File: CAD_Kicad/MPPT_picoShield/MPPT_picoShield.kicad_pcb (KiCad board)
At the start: 2 copper layers, 95 x 65 mm, 61 parts, among them J1 PV_input, J2 Battery_pack, J3 V_out, J4 Micro_SD_Card_Det_Hirose_DM3AT, J5 GPIO breakout, Q1 PMOS_GDS_TO220, Q2 NMOS_DGS_SOT23, Q3 NMOS_DGS_SOT23, SW1 RESET, U1 RaspiPico, U10 LF50_TO220, U2 INA3221

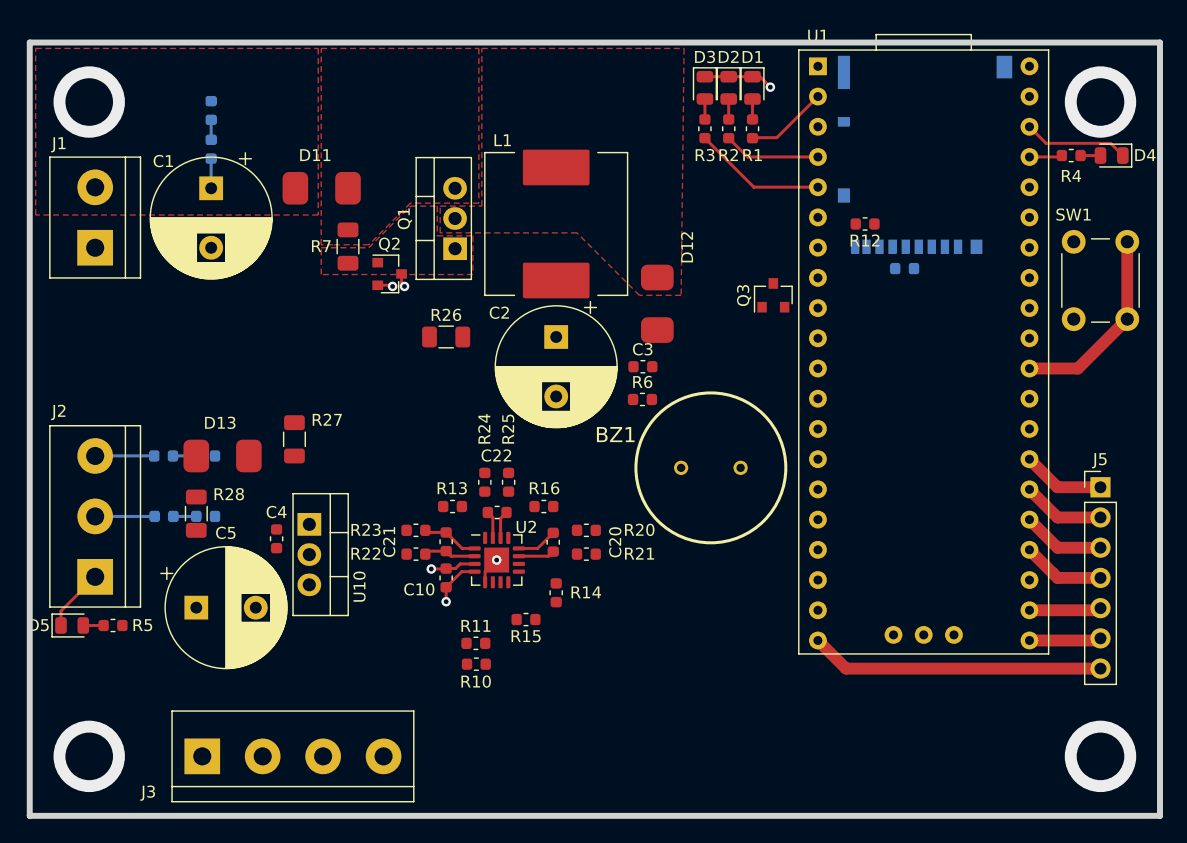
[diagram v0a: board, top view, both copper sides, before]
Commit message: Initial routing
Small verifications to be made: 
- Should Metal of INA2331 be connected to ground? Or a floating metal plane? or Vcc?
- Should capacitors be added to the long analog lines to stabilize them?
- Should D11 and its polarized cap be swapped to "idiot proof" the PV connector?
- Rasp Pico silkscreen is outside of PCB, should probably fix that
- Indicator of pin 1 on INA2331 is overlapping a via, small esthetic fix to be made
- Note for future: DPAK or TO220?
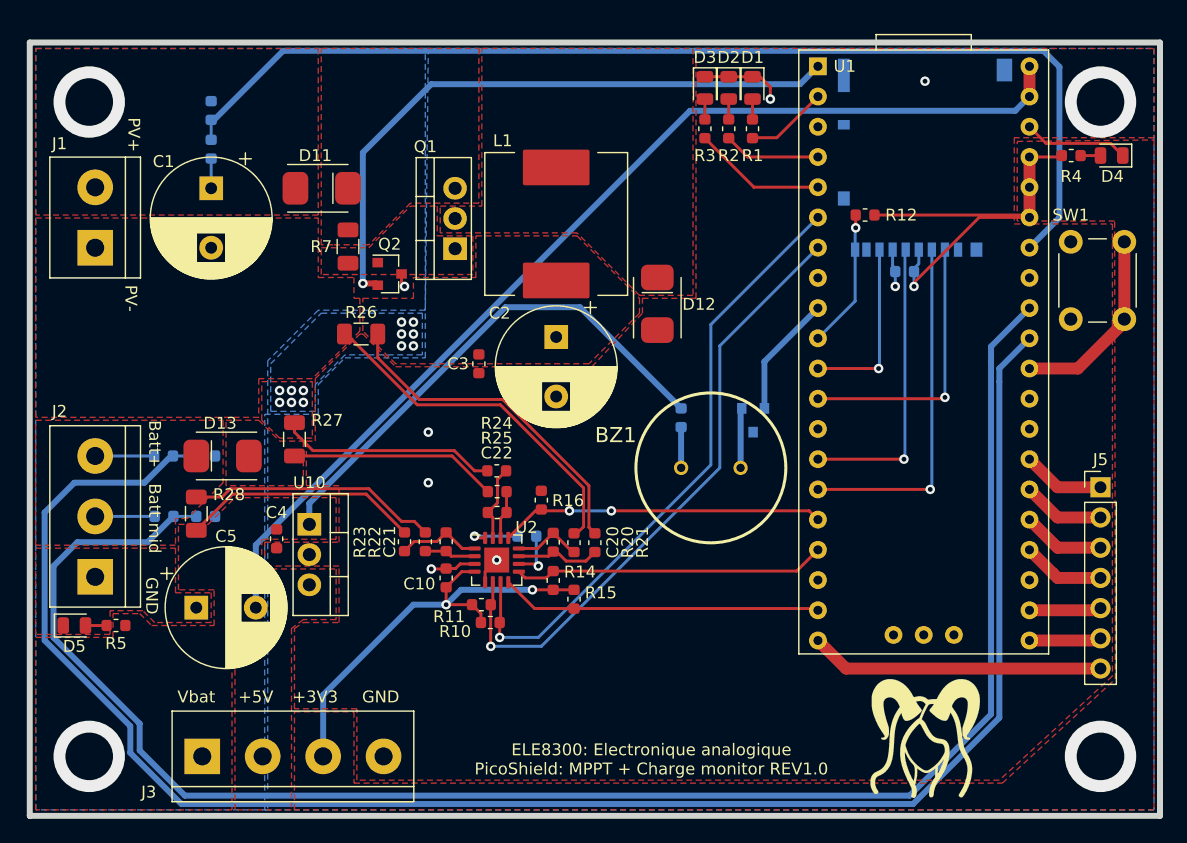
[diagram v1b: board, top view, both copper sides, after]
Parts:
- added G***: LOGO, Custom_MPPT:LogoLucy, F.Cu at (75.2, 58.5)
- Q3, R13, R6: moved to B.Cu
- R30, R32, R34: value 1M -> 1M 1%
- R31: value 50k -> 50k 1%
- R33: value 100k -> 1M 1%
- R35: value 100k -> 470k 1%
- moved C3 13.8 mm to (37.8, 27.0), turned to 270 degrees
- moved Q3 10.6 mm to (60.8, 31.8), turned to 270 degrees
- moved R26 7.15 mm to (27.9, 24.5)
- moved R13 6.73 mm to (41.8, 41.5), turned to 0 degrees
- moved R15 4.39 mm to (45.8, 46.8), turned to 270 degrees
- moved R10 3.69 mm to (38.7, 48.8)
- moved R6 3.60 mm to (54.8, 31.5), turned to 270 degrees
- moved R11 3.28 mm to (38.0, 47.2)
- moved R20 1.47 mm to (45.8, 42.0), turned to 90 degrees
- moved R24 1.39 mm to (39.2, 36.0), turned to 180 degrees
- moved R23 1.36 mm to (31.5, 42.0), turned to 90 degrees
- moved R22 1.30 mm to (33.2, 42.0), turned to 90 degrees
- moved R25 1.24 mm to (39.3, 37.8), turned to 180 degrees
- moved R21 1.20 mm to (47.5, 42.0), turned to 90 degrees
- moved R14 1.07 mm to (44.0, 45.2)
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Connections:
- C21 pad 1: batt_in- -> batt_out-
- C21 pad 2: Batt_in+ -> Batt_out+
- C22 pad 1: batt_out- -> batt_in-
- C22 pad 2: Batt_out+ -> Batt_in+
- R12 pad 1: VCC -> SD_DETECT
- R12 pad 2: SD_DETECT -> VCC
- R22 pad 1: Batt_in+ -> Batt_out+
- R22 pad 2: MPPT_out+ -> Net-(D13-Pad1)
- R23 pad 1: batt_in- -> batt_out-
- R23 pad 2: Net-(D13-Pad2) -> Vbat
- R24 pad 1: Batt_out+ -> Batt_in+
- R24 pad 2: Net-(D13-Pad1) -> MPPT_out+
- R25 pad 1: batt_out- -> batt_in-
- R25 pad 2: Vbat -> Net-(D13-Pad2)
- R30 pad 2: VPV_sense -> Vpv_sense
- R31 pad 1: VPV_sense -> Vpv_sense
- U1 pad 10: TC -> SD_DETECT
- U1 pad 11: WARNING -> SPI_MISO
- U1 pad 12: CRITICAL -> SPI_CS
- U1 pad 16: SPI_MISO -> TC
- U1 pad 17: SPI_CS -> CRITICAL
- U1 pad 19: SD_DETECT -> WARNING
- U2 pad 1: batt_in- -> batt_out-
- U2 pad 14: batt_out- -> batt_in-
- U2 pad 15: Batt_out+ -> Batt_in+
- U2 pad 2: Batt_in+ -> Batt_out+
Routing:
- net VCell2_sense: track 1.96 -> 148.7 mm
- net VCell1_sense: track 1.93 -> 143.7 mm
- net Vpv_sense: track 0.00 -> 92.2 mm
- net +5V: track 0.00 -> 88.4 mm
- net VCC: track 6.91 -> 74.2 mm, vias 1 -> 3
- net Vbat: track 0.00 -> 63.5 mm
- net I2C0_SDA: track 0.00 -> 53.0 mm, vias 0 -> 1
- net I2C0_SCL: track 0.00 -> 52.6 mm, vias 0 -> 1
- net PWM1: track 1.29 -> 53.6 mm
- net MPPT_out+: track 0.00 -> 46.8 mm, vias 0 -> 12
- net SPI_MOSI: track 0.00 -> 29.9 mm, vias 0 -> 1
- net Net-(C1-Pad2): track 0.00 -> 29.7 mm
- net TC: track 0.00 -> 27.3 mm, vias 0 -> 2
- net WARNING: track 0.00 -> 27.0 mm
- net CRITICAL: track 0.00 -> 26.3 mm
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- added copper zone on F.Cu, net +5V
- added copper zone on B.Cu, net MPPT_out+
- added copper zone on F.Cu, net MPPT_out+
- added copper zone on B.Cu, net MPPT_out-
- added copper zone on F.Cu, net MPPT_out-
- added copper zone on F.Cu, net Net-(C1-Pad2)
- added copper zone on F.Cu, net Net-(D13-Pad1)
- added copper zone on F.Cu, net Net-(D13-Pad2)
- added copper zone on F.Cu, net VCC
- added copper zone on F.Cu, net Vbat
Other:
- board text added: "+3V3"
- board text added: "+5V"
- board text added: "Batt mid"
- board text added: "Batt+"
- board text added: "ELE8300: Electronique analogique PicoShield: MPPT + Charge monitor REV1.0"
- board text added: "GND"
- board text added: "PV+"
- board text added: "PV-"
- board text added: "Vbat"

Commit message: Small Changes for hardware "correctability" reasons
Added testpoints
Changed rooting around INA to solve the thermal pad to ground uncertainty. Now able to solve this using an exacto blade
Added PolyMTL logo
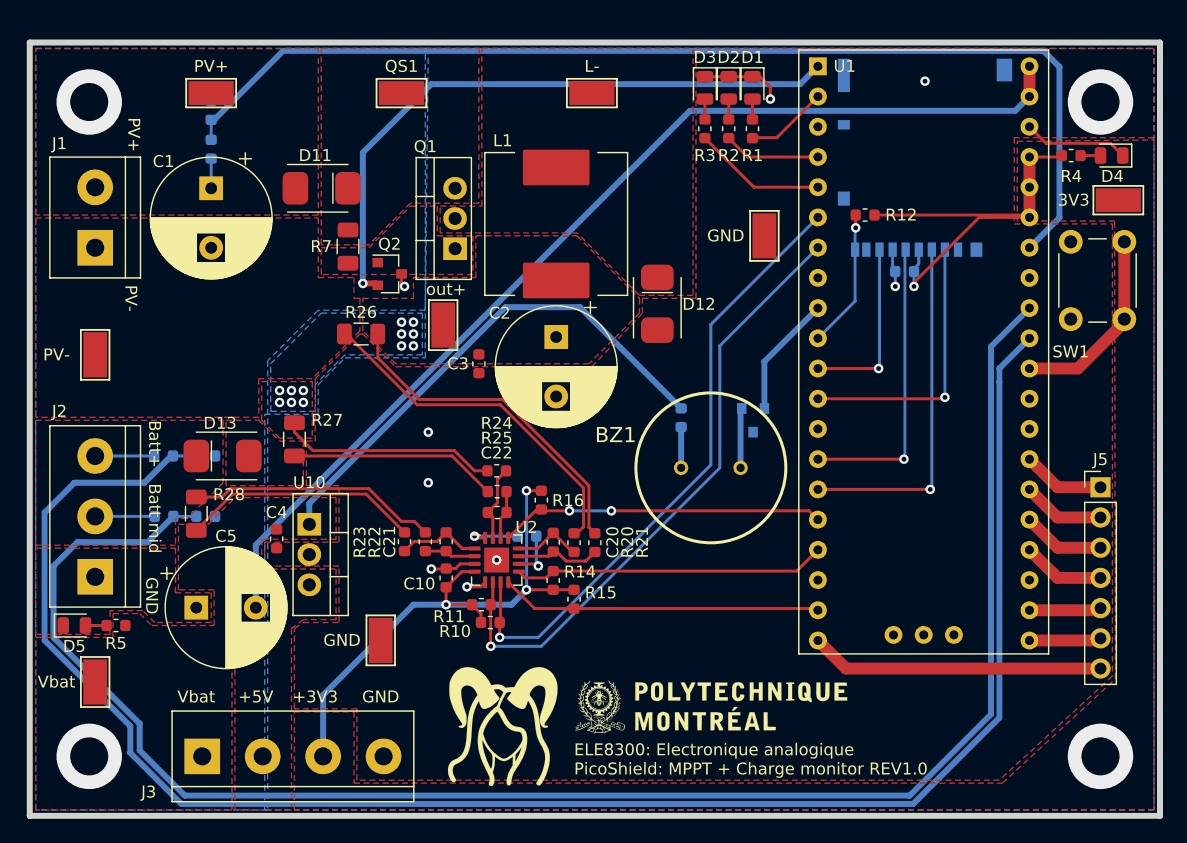
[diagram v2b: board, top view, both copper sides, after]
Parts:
- added 3V3: TestPoint_Keystone_5019_Minature, TestPoint:TestPoint_Keystone_5019_Minature, F.Cu at (91.5, 13.2)
- added G***: LOGO, Custom_MPPT:LogoPOLYMTL, F.Cu at (57.2, 55.8)
- added GND: TestPoint_Keystone_5019_Minature, TestPoint:TestPoint_Keystone_5019_Minature, F.Cu at (29.5, 50.2)
- added GND: TestPoint_Keystone_5019_Minature, TestPoint:TestPoint_Keystone_5019_Minature, F.Cu at (61.8, 16.2)
- added L-: TestPoint_Keystone_5019_Minature, TestPoint:TestPoint_Keystone_5019_Minature, F.Cu at (47.2, 4.25)
- added PV+: TestPoint_Keystone_5019_Minature, TestPoint:TestPoint_Keystone_5019_Minature, F.Cu at (15.2, 4.25)
- added PV-: TestPoint_Keystone_5019_Minature, TestPoint:TestPoint_Keystone_5019_Minature, F.Cu at (5.50, 26.2)
- added QS1: TestPoint_Keystone_5019_Minature, TestPoint:TestPoint_Keystone_5019_Minature, F.Cu at (31.2, 4.25)
- added Vbat: TestPoint_Keystone_5019_Minature, TestPoint:TestPoint_Keystone_5019_Minature, F.Cu at (5.50, 53.8)
- added out+: TestPoint_Keystone_5019_Minature, TestPoint:TestPoint_Keystone_5019_Minature, F.Cu at (34.8, 23.8)
- moved G*** 35.5 mm to (39.8, 57.5)
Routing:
- net VCC: track 74.2 -> 83.9 mm, vias 3 -> 4
- net MPPT_out-: track 26.1 -> 25.5 mm, vias 8 -> 9

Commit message: Gerber gen and added filtering caps on ADC lines
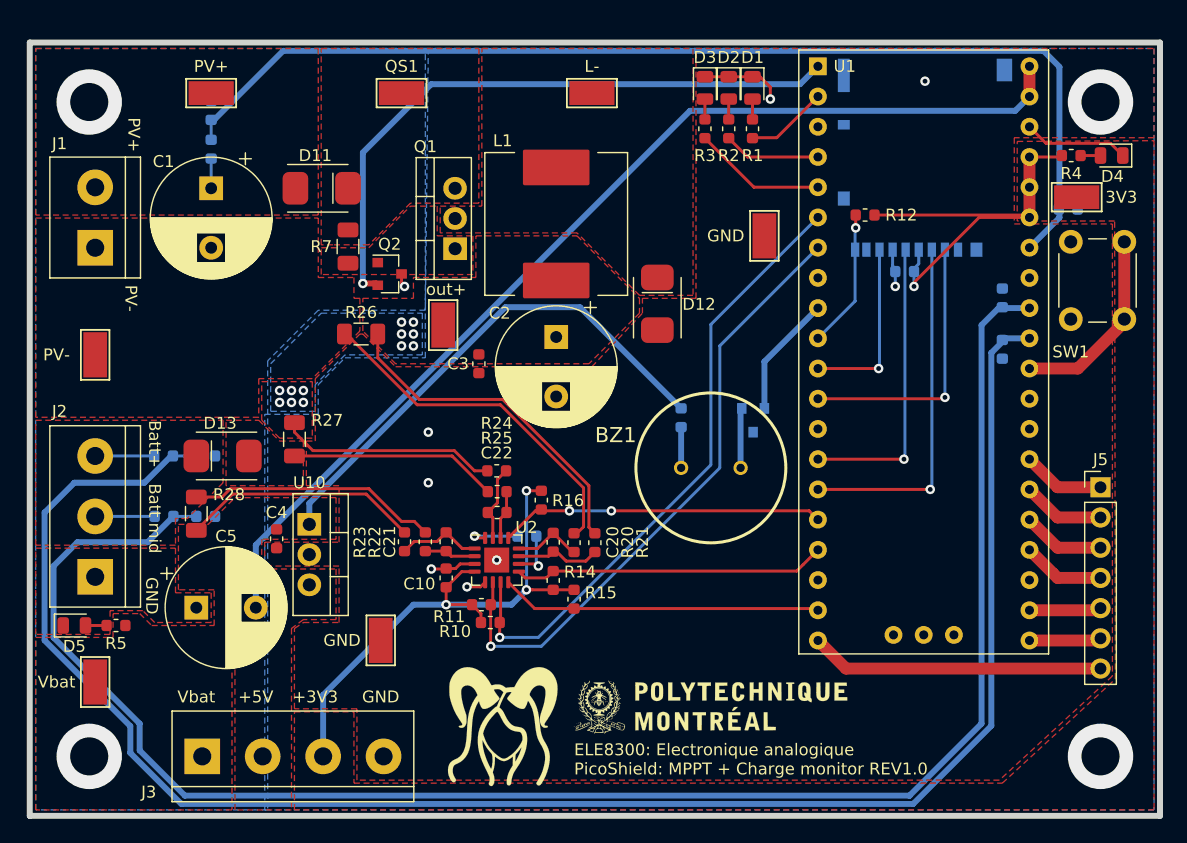
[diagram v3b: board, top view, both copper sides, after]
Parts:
- added C31: .1µF, Capacitor_SMD:C_0603_1608Metric, B.Cu at (87.3, 14.0)
- added C32: .1µF, Capacitor_SMD:C_0603_1608Metric, B.Cu at (81.8, 21.5)
- added C33: .1µF, Capacitor_SMD:C_0603_1608Metric, B.Cu at (81.8, 25.8)
- moved 3V3 3.51 mm to (88.0, 13.0)
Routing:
- net VCell1_sense: track 143.7 -> 145.2 mm
- net VCell2_sense: track 148.7 -> 149.8 mm
